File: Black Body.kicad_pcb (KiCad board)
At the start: 2 copper layers, 52 x 53.7 mm, 39 parts, among them IC2 MCP96L00T-E_MX, J1 53307-2471, J2 Conn_01x02, J3 Conn_01x04, J4 MX150_02x08_RightAngle, J5 Conn_01x06

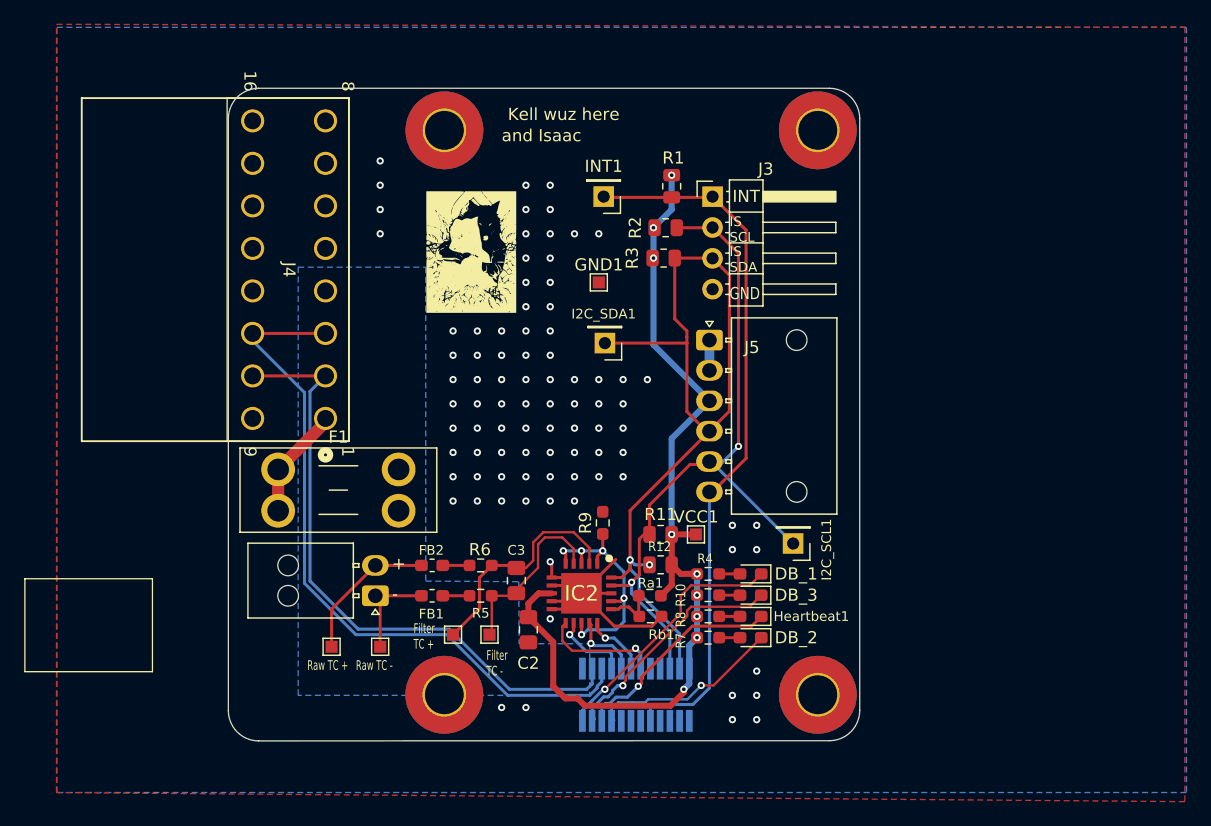
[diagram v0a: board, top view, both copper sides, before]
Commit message: updated silk screen
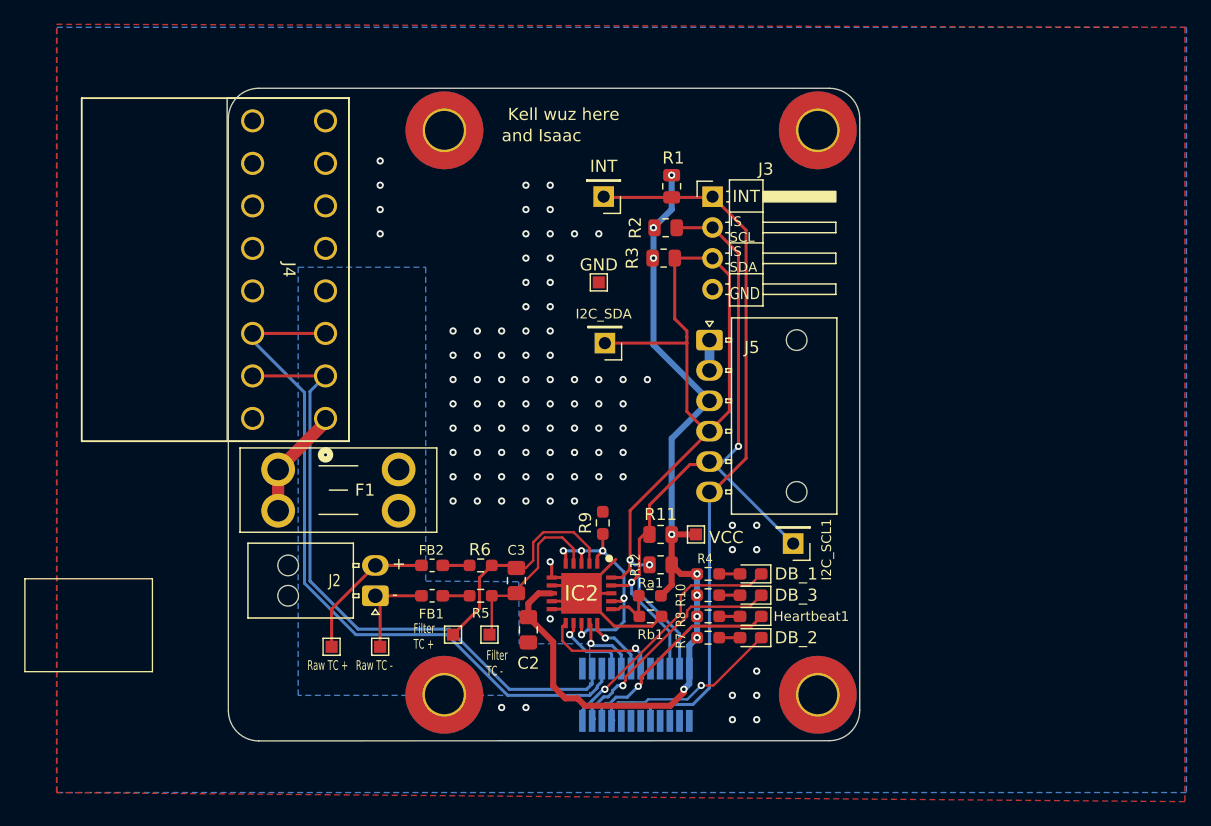
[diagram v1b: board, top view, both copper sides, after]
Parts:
- removed G***: LOGO, LOGO
- renumbered GND1 to GND, I2C_SDA1 to I2C_SDA, INT1 to INT, VCC1 to VCC

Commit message: updated connectors
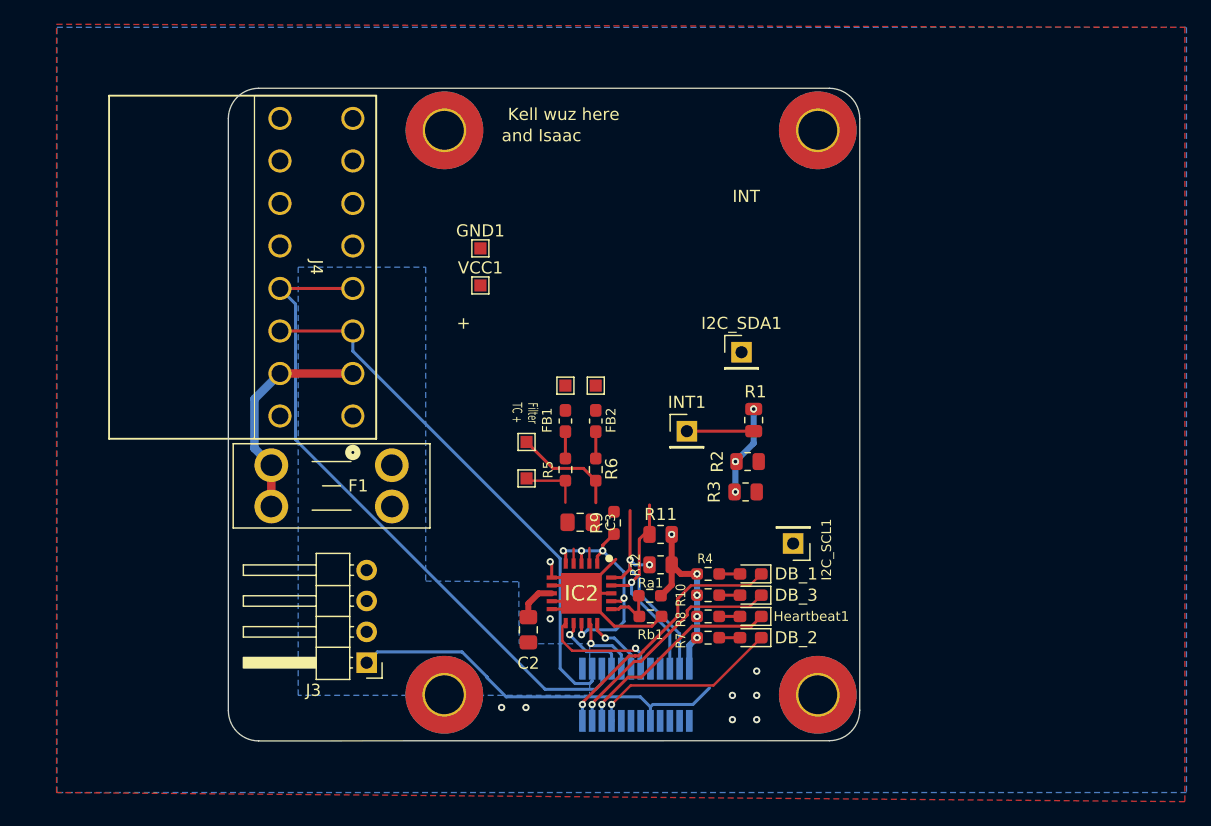
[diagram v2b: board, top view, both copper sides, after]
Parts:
- removed GND, VCC: TestPoint, TestPoint:TestPoint_Pad_1.0x1.0mm
- removed I2C_SDA, INT: TestPoint, Connector_PinHeader_2.54mm:PinHeader_1x01_P2.54mm_Vertical
- removed J2: Conn_01x02, Connector_Molex:Molex_Nano-Fit_105313-xx02_1x02_P2.50mm_Horizontal
- removed J5: Conn_01x06, Connector_Molex:Molex_Nano-Fit_105313-xx06_1x06_P2.50mm_Horizontal
- added GND1: TestPoint, TestPoint:TestPoint_Pad_1.0x1.0mm, F.Cu at (98.2, 80.2)
- added I2C_SDA1: TestPoint, Connector_PinHeader_2.54mm:PinHeader_1x01_P2.54mm_Vertical, F.Cu at (119.8, 88.8)
- added INT1: TestPoint, Connector_PinHeader_2.54mm:PinHeader_1x01_P2.54mm_Vertical, F.Cu at (115.2, 95.2)
- added VCC1: TestPoint, TestPoint:TestPoint_Pad_1.0x1.0mm, F.Cu at (98.2, 83.2)
- moved J3 47.8 mm to (88.9, 114.3), turned to 180 degrees
- moved TP_TC_2 30.6 mm to (107.8, 91.5)
- moved TP_TC_1 26.4 mm to (105.2, 91.5)
- moved R1 20.4 mm to (120.8, 94.3)
- moved R2 20.4 mm to (120.2, 97.8)
- moved R3 20.4 mm to (120.1, 100.2)
- moved FB1 18.1 mm to (105.2, 94.4), turned to -90 degrees
- moved FB2 18.0 mm to (107.8, 94.4), turned to -90 degrees
- moved TP_TC_F_2 17.0 mm to (102.0, 96.1), turned to 90 degrees
- moved TP_TC_F_1 13.2 mm to (102.0, 99.1), turned to 90 degrees
- moved R5 12.5 mm to (105.2, 98.4), turned to 90 degrees
- moved R6 12.3 mm to (107.8, 98.4), turned to 90 degrees
- moved C3 7.11 mm to (106.5, 102.8), turned to 180 degrees
- moved J4 2.26 mm to (84.7, 81.8)
- moved R9 0.92 mm to (109.2, 102.8)
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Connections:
- F1 pad 1: Net-(J4-+24V) -> /temp
- FB1 pad 1: Net-(J2-Pin_1) -> /Temp+
- FB2 pad 1: Net-(J2-Pin_2) -> /Temp-
- J4 pad 1: Net-(J4-+24V) -> /Temp+
- J4 pad 10: /CAN_H -> /temp
- J4 pad 11: /CAN_L -> /CAN_H
- J4 pad 12: GND -> /CAN_L
- J4 pad 13: unconnected-(J4-Pad13) -> GND
- J4 pad 14: unconnected-(J4-Pad14) -> GND
- J4 pad 15: unconnected-(J4-Pad15) -> /I2C1_SDA
- J4 pad 2: /CAN_H -> /temp
- J4 pad 3: /CAN_L -> /CAN_H
- J4 pad 4: +24V -> /CAN_L
- J4 pad 5: unconnected-(J4-Pad5) -> GND
- J4 pad 6: unconnected-(J4-Pad6) -> +3V3
- J4 pad 7: unconnected-(J4-Pad7) -> /I2C1_SCL
- J4 pad 8: unconnected-(J4-Pad8) -> /INT
- J4 pad 9: GND -> /Temp-
- TP_TC_1 pad 1: Net-(J2-Pin_1) -> /Temp+
- TP_TC_2 pad 1: Net-(J2-Pin_2) -> /Temp-
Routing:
- net /I2C1_SDA: track 69.6 -> 19.3 mm
- net +3V3: track 75.7 -> 27.2 mm, vias 9 -> 8
- net /I2C1_SCL: track 59.5 -> 17.6 mm, vias 2 -> 1
- net /INT: track 59.0 -> 38.3 mm
- net /temp: track 0.00 -> 18.4 mm
- net Net-(J2-Pin_2): track 11.7 -> 0.00 mm
- net Net-(IC2-VIN+): track 19.4 -> 10.1 mm
- net Net-(J4-+24V): track 9.22 -> 0.00 mm
- net Net-(IC2-VIN-): track 15.6 -> 6.71 mm
- net Net-(J2-Pin_1): track 7.97 -> 0.00 mm
- net /CAN_H: track 52.3 -> 45.1 mm
- net /CAN_L: track 58.3 -> 54.1 mm
- net GND: track 23.4 -> 20.9 mm, vias 88 -> 9
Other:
- board text removed: "-"
- board text removed: "Filter TC -"
- board text removed: "GND"
- board text removed: "IS SCL"
- board text removed: "IS SDA"
- board text removed: "Raw TC +"
- board text removed: "Raw TC -"

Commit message: updated connectors
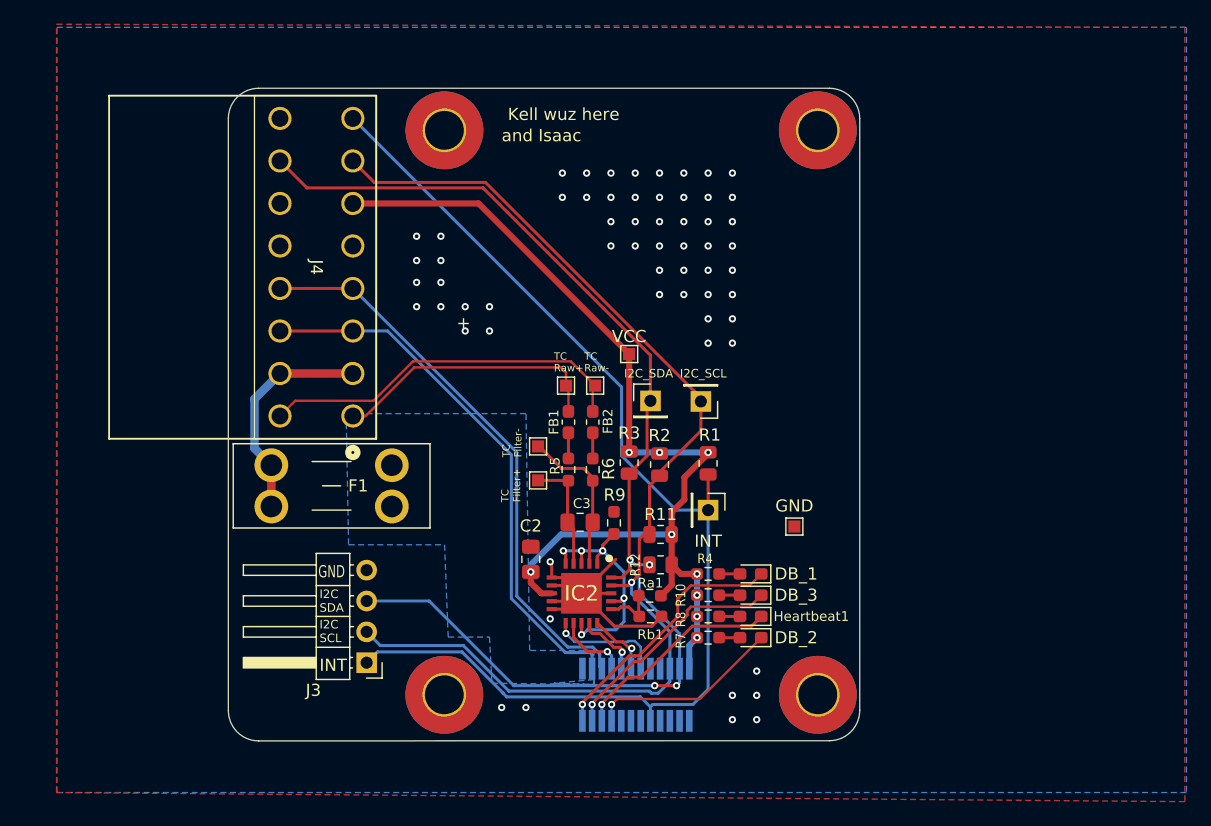
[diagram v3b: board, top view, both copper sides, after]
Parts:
- moved GND 34.5 mm to (124.1, 103.1)
- moved I2C_SCL 14.0 mm to (116.4, 92.8)
- moved VCC 13.5 mm to (110.5, 88.9)
- moved R3 9.89 mm to (110.5, 97.8), turned to -90 degrees
- moved I2C_SDA 8.50 mm to (112.2, 92.8)
- moved R2 7.25 mm to (113.0, 98.0), turned to -90 degrees
- moved INT 6.73 mm to (117.0, 101.8), turned to -90 degrees
- moved C2 5.80 mm to (102.4, 105.8), turned to -90 degrees
- moved R1 5.17 mm to (117.0, 97.9)
- moved TP_TC_F_2 1.02 mm to (103.0, 96.5)
- moved TP_TC_F_1 0.96 mm to (103.0, 99.3)
- moved FB1 0.26 mm to (105.5, 94.5)
- moved FB2 0.26 mm to (107.5, 94.5)
- moved R5 0.25 mm to (105.5, 98.4)
- moved R6 0.25 mm to (107.5, 98.4)
- renumbered GND1 to GND, I2C_SCL1 to I2C_SCL, I2C_SDA1 to I2C_SDA, INT1 to INT, VCC1 to VCC
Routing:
- net /I2C1_SDA: track 19.3 -> 99.8 mm, vias 2 -> 4
- net /I2C1_SCL: track 17.6 -> 93.9 mm
- net /INT: track 38.3 -> 95.7 mm
- net +3V3: track 27.2 -> 82.8 mm, vias 8 -> 9
- net /Temp-: track 0.00 -> 30.9 mm
- net /Temp+: track 0.12 -> 22.7 mm
- net /CAN_L: track 54.1 -> 47.0 mm
- net Net-(IC2-VIN-): track 6.71 -> 10.1 mm
- net Net-(IC2-VIN+): track 10.1 -> 12.9 mm
- net /Alert_1: track 9.95 -> 9.39 mm
- net GND: vias 9 -> 61
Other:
- board text added: "GND"
- board text added: "I2C SCL"
- board text added: "I2C SDA"
- board text added: "TC Filter+"
- board text added: "TC Filter-"
- board text added: "TC Raw+"
- board text added: "TC Raw-"
- board text removed: "Filter TC +"

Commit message: updated BOM
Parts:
- moved TP_TC_F_2 0.53 mm to (102.5, 96.5)
- moved TP_TC_F_1 0.50 mm to (102.5, 99.3)
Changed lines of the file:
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@@
 			(outputformat 1)
 			(mirror no)
-			(drillshape 1)
+			(drillshape 0)
 			(scaleselection 1)
 			(outputdirectory "")
@@
 		(tags "resistor handsolder")
 		(property "Reference" "R6"
-			(at 0.0625 1.302 90)
+			(at 0.0625 1.5 90)
 			(layer "F.SilkS")
 			(effects
@@
 	(footprint "TestPoint:TestPoint_Pad_1.0x1.0mm"
 		(layer "F.Cu")
-		(at 103 96.5 90)
+		(at 102.475 96.5 90)
 		(descr "SMD rectangular pad as test Point, square 1.0mm side length")
 		(tags "test point SMD pad rectangle square")
@@
 	(footprint "TestPoint:TestPoint_Pad_1.0x1.0mm"
 		(layer "F.Cu")
-		(at 103 99.3 90)
+		(at 102.5 99.35 90)
 		(descr "SMD rectangular pad as test Point, square 1.0mm side length")
 		(tags "test point SMD pad rectangle square")
@@
 		(tags "resistor handsolder")
 		(property "Reference" "R5"
-			(at 0.3125 -1.1 90)
+			(at 0.4375 -1.35 90)
 			(layer "F.SilkS")
 			(effects
@@
 	)
 	(gr_text "TC\nFilter-\n"
-		(at 101.7 97.4 90)
+		(at 101.425 97.75 90)
 		(layer "F.SilkS")
 		(effects
@@
 		(width 0.25)
 		(layer "F.Cu")
+		(net 28)
+	)
+	(segment
+		(start 102.5 99.5)
+		(end 102.8 99.5)
+		(width 0.25)
+		(layer "F.Cu")

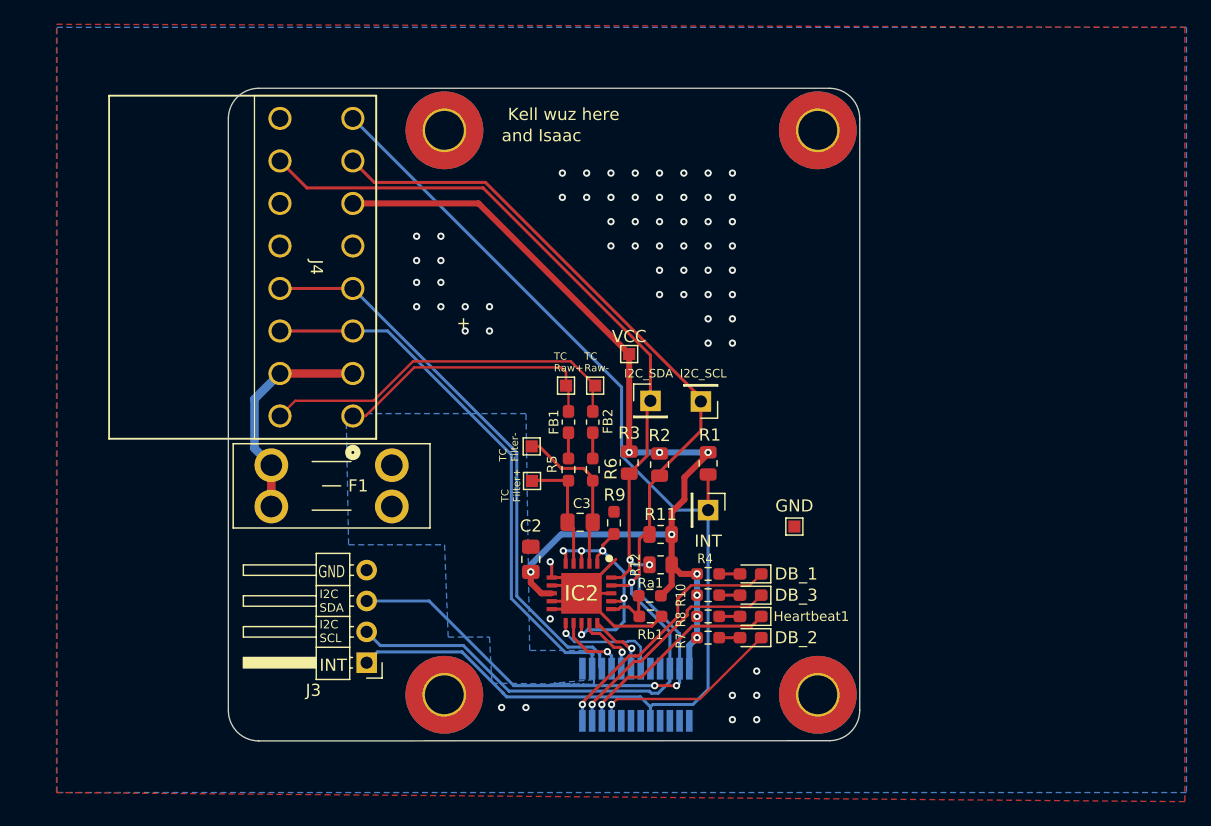
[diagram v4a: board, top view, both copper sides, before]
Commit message: moved fuse
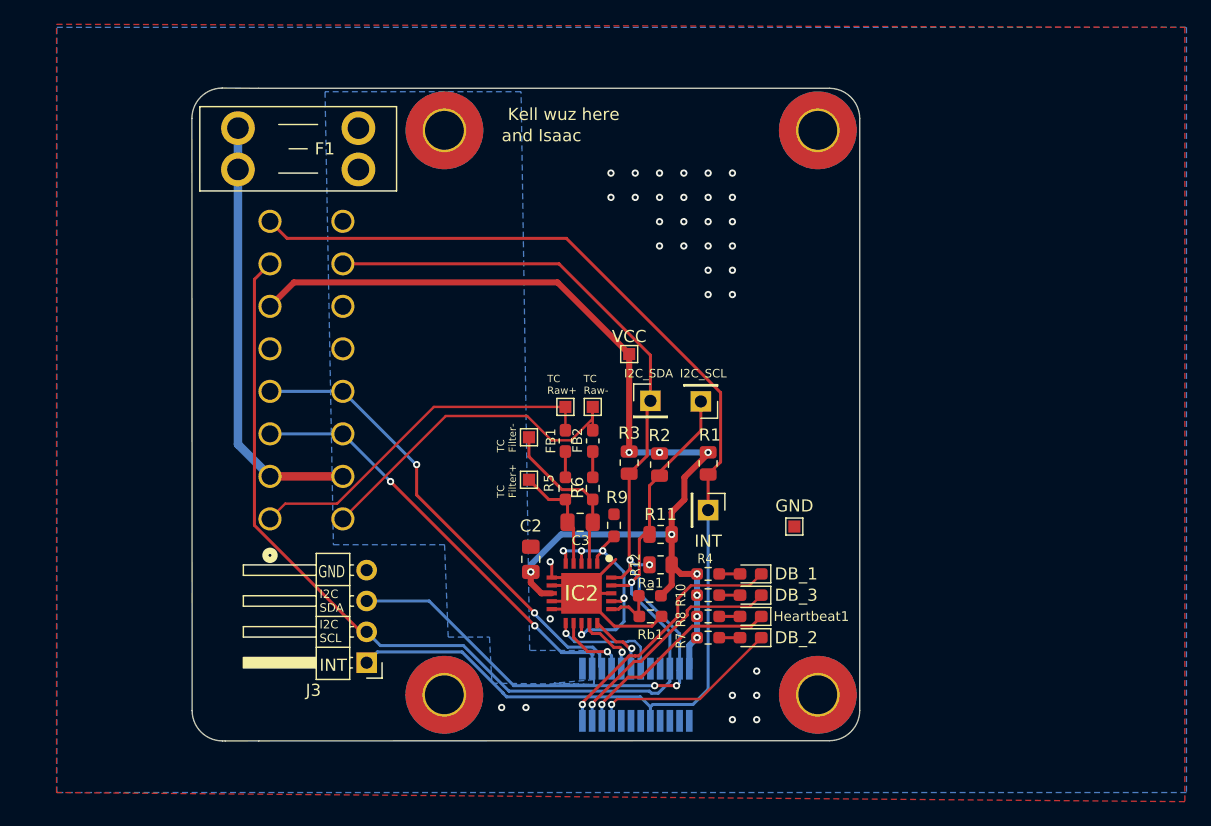
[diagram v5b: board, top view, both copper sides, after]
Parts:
- J4: moved to B.Cu
- moved F1 27.9 mm to (78.3, 70.3)
- moved J4 8.51 mm to (83.9, 90.3)
- moved TP_TC_2 1.76 mm to (107.5, 93.2)
- moved TP_TC_1 1.75 mm to (105.2, 93.2)
- moved R5 1.57 mm to (105.2, 100.0)
- moved FB1 1.57 mm to (105.2, 96.0)
- moved R6 1.55 mm to (107.5, 100.0)
- moved FB2 1.55 mm to (107.5, 96.0)
- moved TP_TC_F_2 0.78 mm to (102.2, 95.8)
- moved TP_TC_F_1 0.27 mm to (102.2, 99.2)
- moved R9 0.20 mm to (109.2, 103.0)
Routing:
- net /temp: track 18.4 -> 35.8 mm
- net /CAN_H: track 44.8 -> 35.2 mm, vias 0 -> 2
- net /I2C1_SDA: track 99.8 -> 91.2 mm
- net /CAN_L: track 47.0 -> 38.9 mm, vias 0 -> 2
- net /Temp+: track 22.7 -> 30.1 mm
- net +3V3: track 82.8 -> 87.8 mm
- net /INT: track 95.7 -> 99.9 mm
- net /Temp-: track 30.9 -> 28.5 mm
- net /I2C1_SCL: track 93.9 -> 92.1 mm
- net Net-(IC2-VIN-): track 10.4 -> 9.33 mm
- net Net-(IC2-VIN+): track 12.9 -> 13.7 mm
- net GND: vias 61 -> 33
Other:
- board size 52 x 53.7 mm -> 55 x 53.8 mm
- board text removed: "+"

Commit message: better file system
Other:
- board size 55 x 53.8 mm -> 55.5 x 53.8 mm
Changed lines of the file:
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@@
 		(at 111.05 116.95)
 		(property "Reference" "J1"
-			(at 6.8 -0.67 270)
+			(at 6.8 -0.67 90)
 			(layer "B.SilkS")
 			(effects
@@
 		)
 		(property "Value" "53307-2471"
-			(at 6.5278 5.08 180)
+			(at 6.5278 5.08 0)
 			(layer "B.Fab")
 			(effects
@@
 		)
 		(property "Datasheet" "https://www.molex.com/en-us/products/part-detail-pdf/533072471?display=pdf"
-			(at 0 0 180)
+			(at 0 0 0)
 			(layer "B.Fab")
 			(hide yes)
@@
 		)
 		(property "Description" "Board-to-board connector for Peripheral SOM daughterboards"
-			(at 0 0 180)
+			(at 0 0 0)
 			(layer "B.Fab")
 			(hide yes)
@@
 		)
 		(fp_text user "533072471"
-			(at -5.1816 6.35 180)
+			(at -5.1816 6.35 0)
 			(layer "B.Fab")
 			(effects
@@
 		)
 	)
-	(gr_line
-		(start 77 67)
-		(end 80 67.017767)
-		(stroke
-			(width 0.05)
-			(type default)
-		)
-		(layer "Edge.Cuts")
-	)
 	(gr_arc
 		(start 129.482233 118.232233)
@@
 		(layer "Edge.Cuts")
 	)
-	(gr_line
-		(start 77.25 120.75104)
-		(end 77.017767 120.751128)
-		(stroke
-			(width 0.05)
-			(type default)
-		)
-		(layer "Edge.Cuts")
-	)
-	(gr_line
-		(start 80 120.75)
-		(end 126.982233 120.732233)
-		(stroke
-			(width 0.05)
-			(type default)
-		)
-		(layer "Edge.Cuts")
-	)
 	(gr_arc
 		(start 126.982254 67.017755)
@@
 		(layer "Edge.Cuts")
 	)
-	(gr_line
-		(start 74.5 69.5)
-		(end 74.517767 118.25)
+	(gr_arc
+		(start 74 69.5)
+		(mid 74.732233 67.732233)
+		(end 76.5 67)
 		(stroke
 			(width 0.05)
@@
 		(layer "Edge.Cuts")
 	)
-	(gr_arc
-		(start 74.5 69.5)
-		(mid 75.232233 67.732233)
-		(end 77 67)
+	(gr_line
+		(start 129.482233 118.232233)
+		(end 129.482254 69.517755)
 		(stroke
 			(width 0.05)
@@
 	)
 	(gr_line
-		(start 129.482233 118.232233)
-		(end 129.482254 69.517755)
+		(start 126.9822 67.017755)
+		(end 76.5 67)
 		(stroke
 			(width 0.05)
@@
 	)
 	(gr_line
-		(start 80 67.017767)
-		(end 126.982254 67.017755)
+		(start 76.51779 120.75)
+		(end 126.982233 120.732233)
 		(stroke
 			(width 0.05)
@@
 		(layer "Edge.Cuts")
 	)
-	(gr_arc
-		(start 77.017767 120.75)
-		(mid 75.25 120.017767)
-		(end 74.517767 118.25)
+	(gr_line
+		(start 74 69.5)
+		(end 74.017767 118.25)
 		(stroke
 			(width 0.05)
@@
 		(layer "Edge.Cuts")
 	)
-	(gr_line
-		(start 80 120.75)
-		(end 77.25 120.75104)
+	(gr_arc
+		(start 76.517767 120.75)
+		(mid 74.75 120.017767)
+		(end 74.017767 118.25)
 		(stroke
 			(width 0.05)
@@
 			)
 		)
+	)
+	(zone
+		(net 37)
+		(net_name "/INT")
+		(layer "B.Cu")
+		(name "$teardrop_padvia$")
+		(hatch none 0.1)
+		(priority 30000)
+		(attr
+			(teardrop
+				(type padvia)
+			)
+		)
+		(connect_pads yes
+			(clearance 0)
+		)
+		(min_thickness 0.0254)
+		(filled_areas_thickness no)
+		(fill yes
+			(thermal_gap 0.5)
+			(thermal_bridge_width 0.5)
+			(island_removal_mode 1)
+			(island_area_min 10)
+		)
+		(polygon
+			(pts
+				(xy 98.368253 114.874958) (xy 98.191476 115.051735) (xy 97.611064 114.219905) (xy 96.070707 116.950707)
+				(xy 98.948666 115.706789)
+			)
+		)
